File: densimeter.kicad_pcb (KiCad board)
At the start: 2 copper layers, 3 parts, among them IC1 XGZP6897A

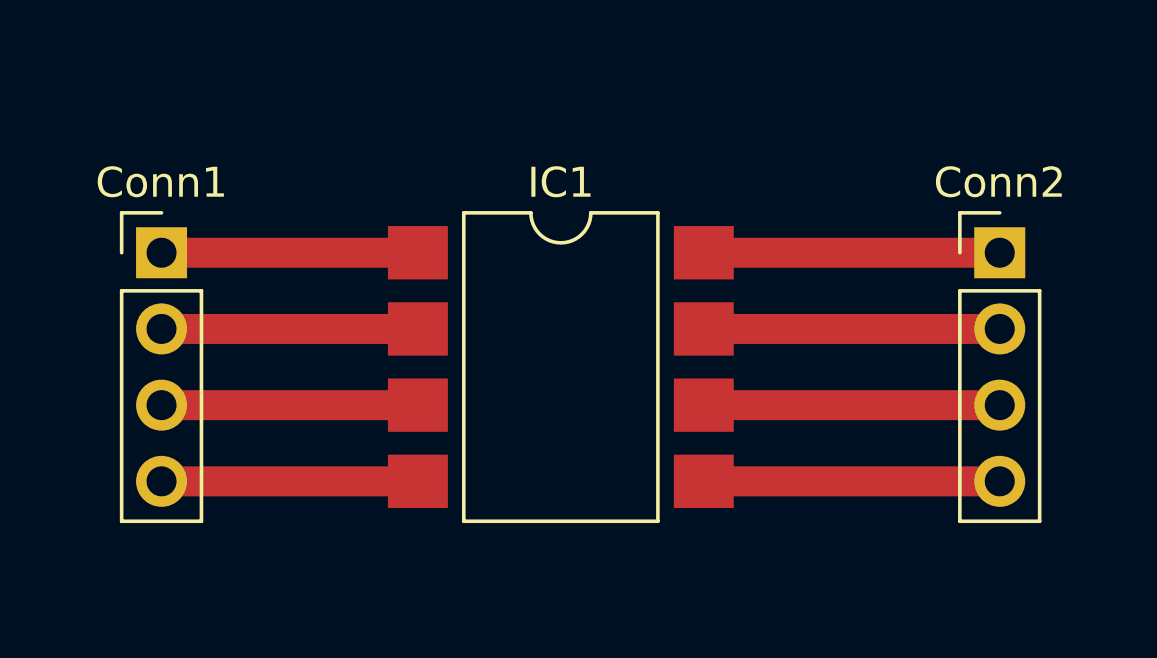
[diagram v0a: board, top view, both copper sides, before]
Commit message: added 100 nF capacitor C1
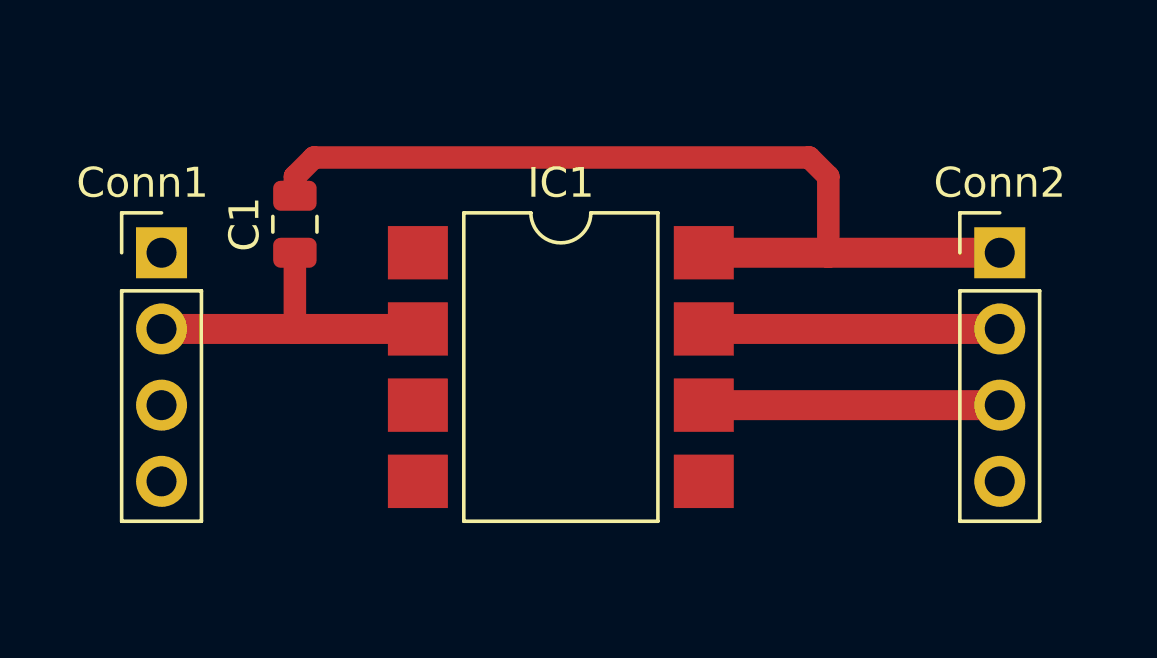
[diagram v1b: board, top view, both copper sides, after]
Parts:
- added C1: 100 nF, Capacitor_SMD:C_0805_2012Metric, F.Cu at (3.17, 7.94)
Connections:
- net Net-(Conn1-Pad2) renamed /Vdd
- net Net-(Conn2-Pad1) renamed /GND
- net Net-(Conn2-Pad2) renamed /SCL
- net Net-(Conn2-Pad3) renamed /SDA
- Conn1 pad 1: Net-(Conn1-Pad1) -> (no net)
- Conn1 pad 3: Net-(Conn1-Pad3) -> (no net)
- Conn1 pad 4: Net-(Conn1-Pad4) -> (no net)
- Conn2 pad 4: Net-(Conn2-Pad4) -> (no net)
- IC1 pad 1: Net-(Conn1-Pad1) -> (no net)
- IC1 pad 3: Net-(Conn1-Pad3) -> (no net)
- IC1 pad 4: Net-(Conn1-Pad4) -> (no net)
- IC1 pad 5: Net-(Conn2-Pad4) -> (no net)
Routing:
- net /GND: track 8.89 -> 30.4 mm
- net Net-(Conn2-Pad4): track 8.89 -> 0.00 mm
- net Net-(Conn1-Pad4): track 7.57 -> 0.00 mm
- net Net-(Conn1-Pad3): track 7.57 -> 0.00 mm
- net Net-(Conn1-Pad1): track 7.57 -> 0.00 mm
- net /Vdd: track 7.57 -> 10.1 mm

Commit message: 4 pins module
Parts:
- removed Conn2: CONN_4X1, Connector_PinHeader_2.54mm:PinHeader_1x04_P2.54mm_Vertical
- moved Conn1 26.7 mm to (25.4, 7.62)
- moved IC1 1.43 mm to (12.7, 11.4)
- moved C1 0.90 mm to (3.81, 7.30)
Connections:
- C1 pad 2: /GND -> /Gnd
- Conn1 pad 1: (no net) -> /SCL
- Conn1 pad 2: /Vdd -> /SDA
- Conn1 pad 3: (no net) -> /Vdd
- Conn1 pad 4: (no net) -> /Gnd
- IC1 pad 8: /GND -> /Gnd
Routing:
- net /Gnd: track 0.00 -> 41.7 mm
- net /Vdd: track 10.1 -> 40.6 mm
- net /GND: track 30.4 -> 0.00 mm
- net /SDA: track 8.89 -> 9.73 mm
- net /SCL: track 8.89 -> 9.73 mm
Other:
- board outline added: 27.3 x 17.1 mm
- board text added: "GND"
- board text added: "SCL"
- board text added: "SDA"
- board text added: "Vdd"

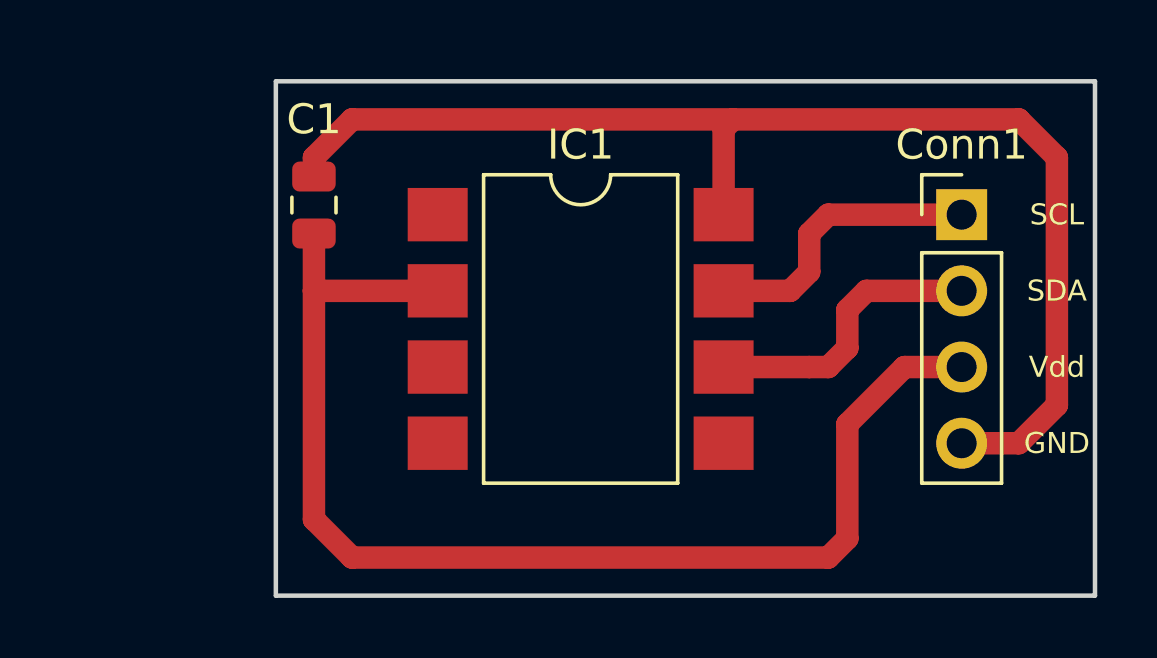
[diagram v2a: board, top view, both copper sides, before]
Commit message: pull up resistors added
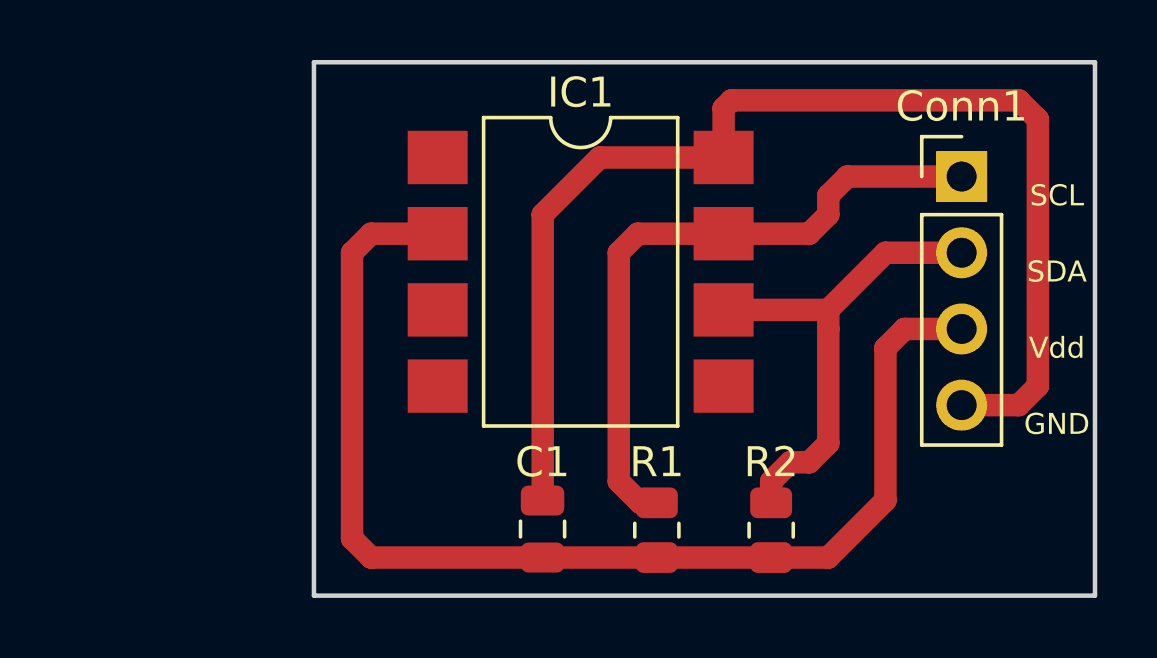
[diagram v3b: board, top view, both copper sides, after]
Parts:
- added R1: 4.7 k, Resistor_SMD:R_0805_2012Metric, F.Cu at (15.2, 18.1)
- added R2: 4.7 k, Resistor_SMD:R_0805_2012Metric, F.Cu at (19.1, 18.1)
- moved C1 13.2 mm to (11.4, 18.1)
- moved IC1 1.90 mm to (12.7, 9.53)
- moved Conn1 1.27 mm to (25.4, 6.35)
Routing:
- net /SCL: track 9.73 -> 22.0 mm
- net /SDA: track 9.73 -> 16.3 mm
- net /Vdd: track 40.6 -> 39.4 mm
- net /Gnd: track 41.7 -> 40.5 mm
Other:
- board size 27.3 x 17.1 mm -> 26 x 17.8 mm
